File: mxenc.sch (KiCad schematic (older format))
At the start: 35 parts, among them J10 Conn_02x05_Odd_Even, J4 Conn_01x06, J6 Conn_01x06, J8 Conn_01x04_MountingPin, SW1 SW_Push, SW2 SW_Push, SW3 SW_Push, U1 IMX8MM, U10 24C32, Y2 Crystal_GND24

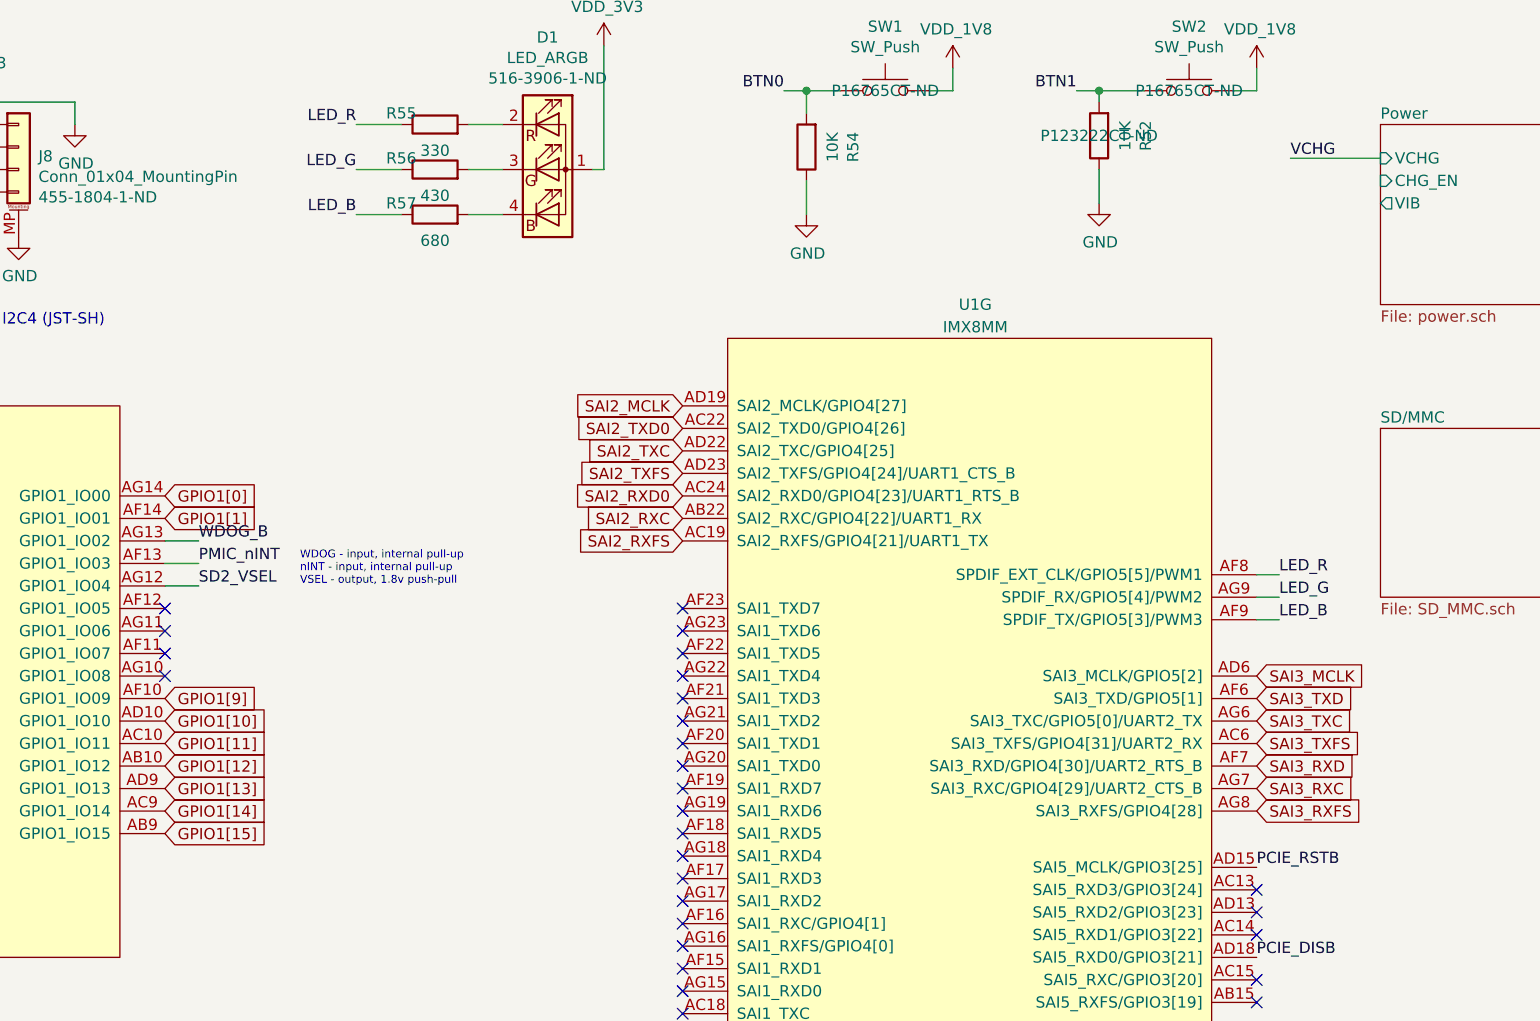
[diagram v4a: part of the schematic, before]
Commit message: Cleanup remaining DRC problems from schematic
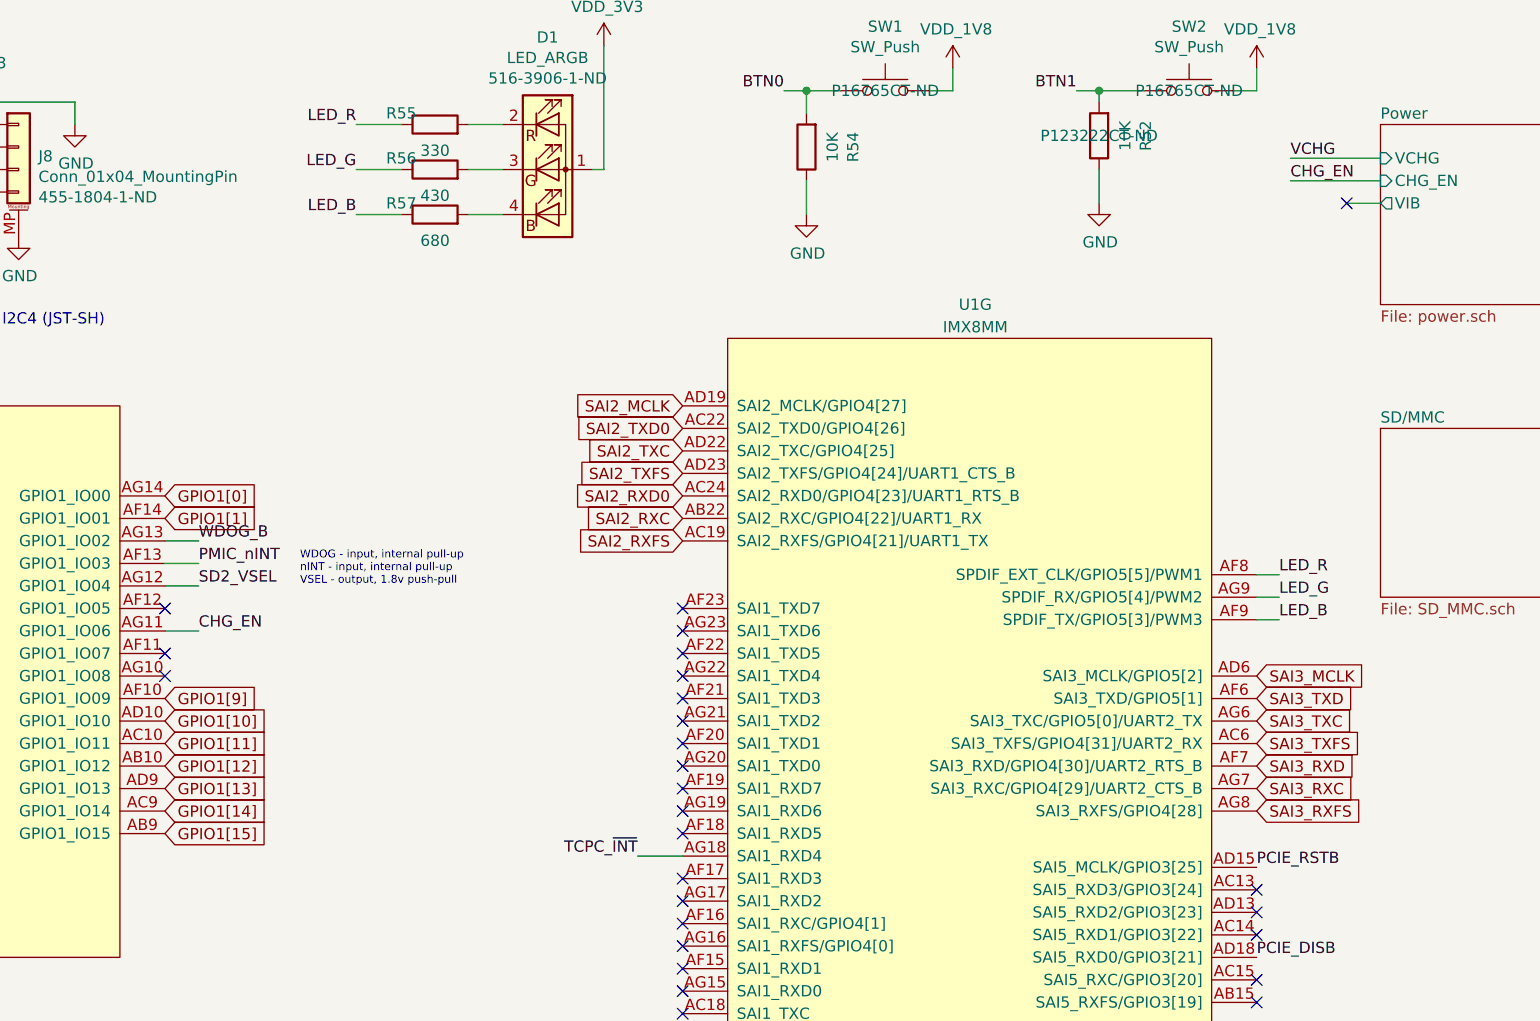
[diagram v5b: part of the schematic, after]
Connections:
- net TCPC_~INT: now also U1.AG18 (SAI1_RXD4)
- net CHG_EN: now reaches U1.AG11 (GPIO1_IO06)
- no-connect marks 37 -> 36
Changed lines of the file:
@@
 	1    0    0    -1
 $EndComp
-NoConn ~ 5600 3550
 NoConn ~ 5600 3650
 Wire Wire Line
@@
 NoConn ~ 7900 4350
 NoConn ~ 7900 4450
-NoConn ~ 7900 4550
 NoConn ~ 7900 4650
 NoConn ~ 7900 4750
@@
 NoConn ~ 3500 1500
 NoConn ~ 3500 1600
+NoConn ~ 10850 1650
+Wire Wire Line
+	11000 1650 10850 1650
+Text Label 7700 4550 2    50   ~ 0
+TCPC_~INT
+Wire Wire Line
+	7700 4550 7900 4550
+Text Label 10600 1550 0    50   ~ 0
+CHG_EN
+Wire Wire Line
+	10600 1550 11000 1550
+Text Label 5750 3550 0    50   ~ 0
+CHG_EN
+Wire Wire Line
+	5750 3550 5600 3550
 $EndSCHEMATC

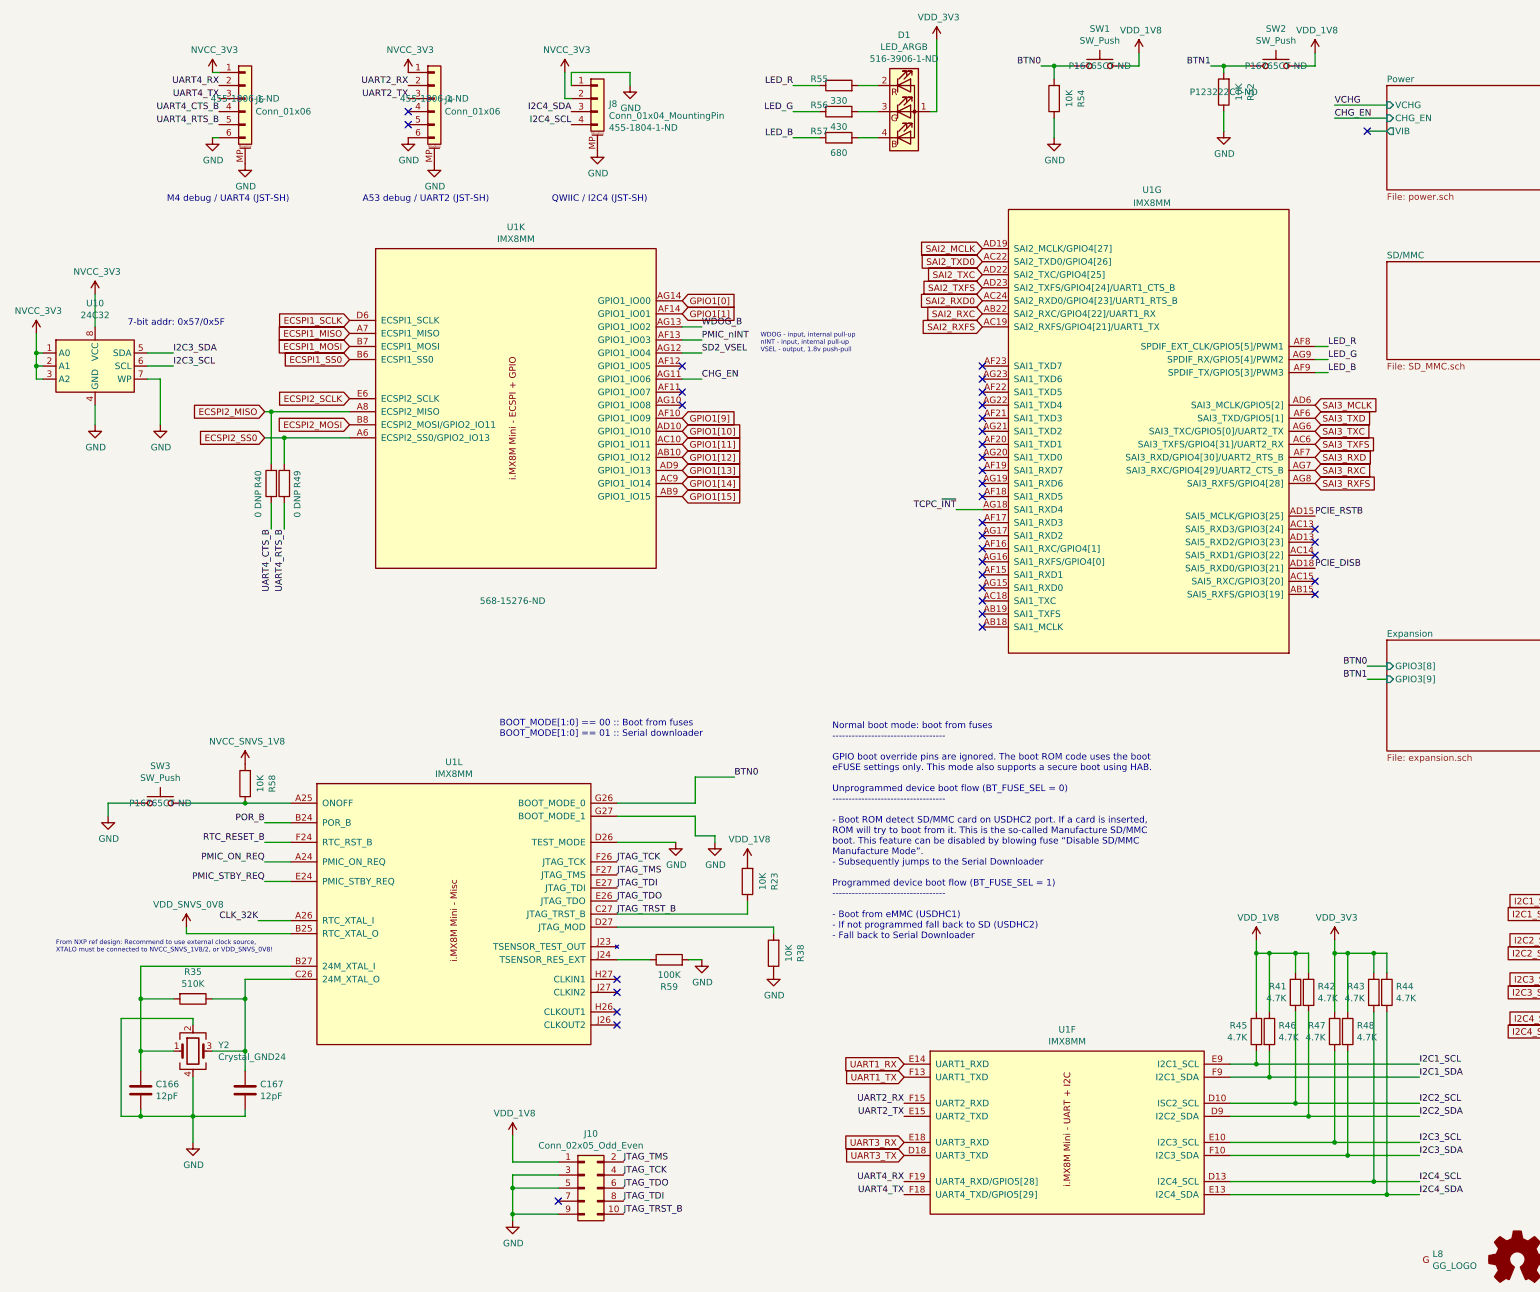
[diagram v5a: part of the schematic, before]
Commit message: Re-annotate schematics, add dnp field, and silkscreen cleanup
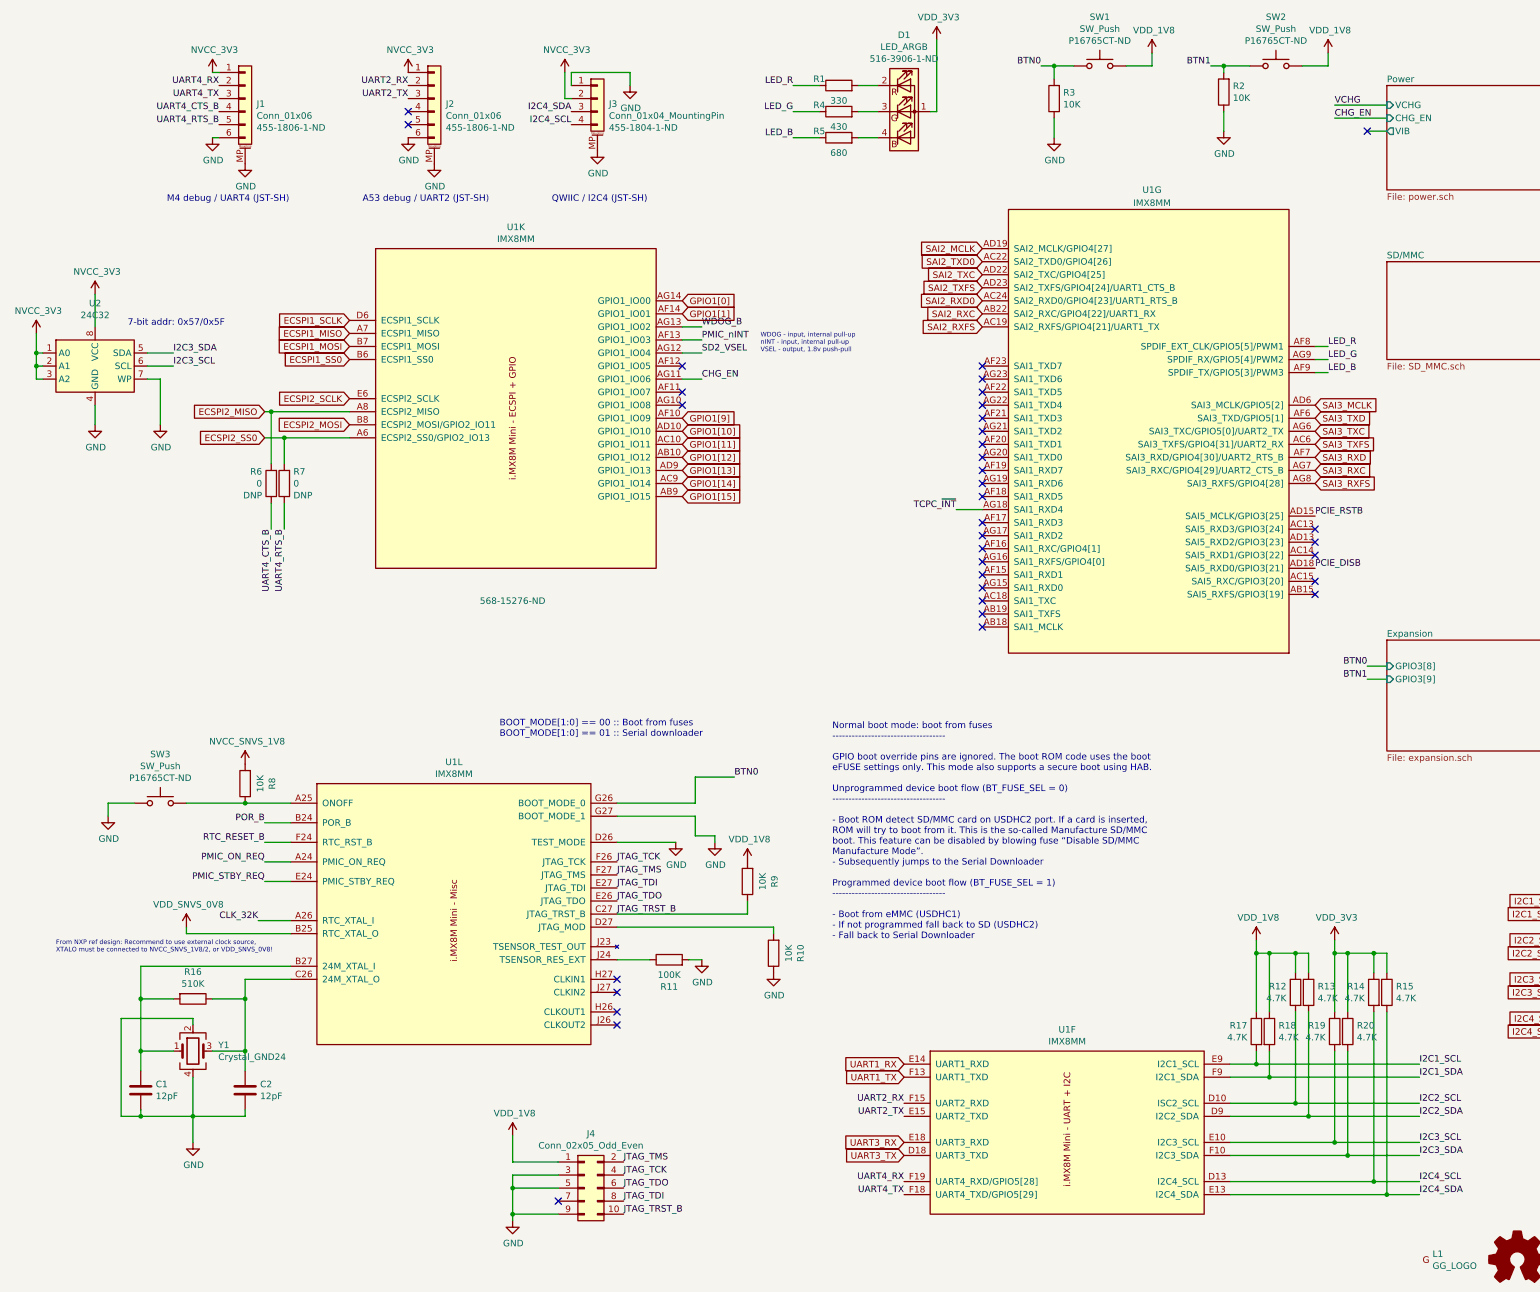
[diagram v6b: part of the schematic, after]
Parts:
- J4: renamed from J10; Populate (none) -> DNP
- L1: renamed from L8; Populate (none) -> DNP
- LOGO1: Populate (none) -> DNP
- R6: renamed from R40; value 0 DNP -> 0; Populate (none) -> DNP
- R7: renamed from R49; value 0 DNP -> 0; Populate (none) -> DNP
- renumbered C166 to C1, C167 to C2, J6 to J1, J4 to J2, J8 to J3, R55 to R1, R38 to R10, R59 to R11, R41 to R12, R42 to R13, R43 to R14, R44 to R15, R35 to R16, R45 to R17, R46 to R18, R47 to R19, R52 to R2, R48 to R20, R54 to R3, R56 to R4, R57 to R5, R58 to R8, R23 to R9, U10 to U2, Y2 to Y1
